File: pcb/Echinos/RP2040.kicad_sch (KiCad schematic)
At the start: 28 parts, among them SW224 Boot, SW225 Boot, SW226 Reset, SW227 Reset, U200 W25Q128JVP, U201 RP2040, Y200 Crystal_GND24

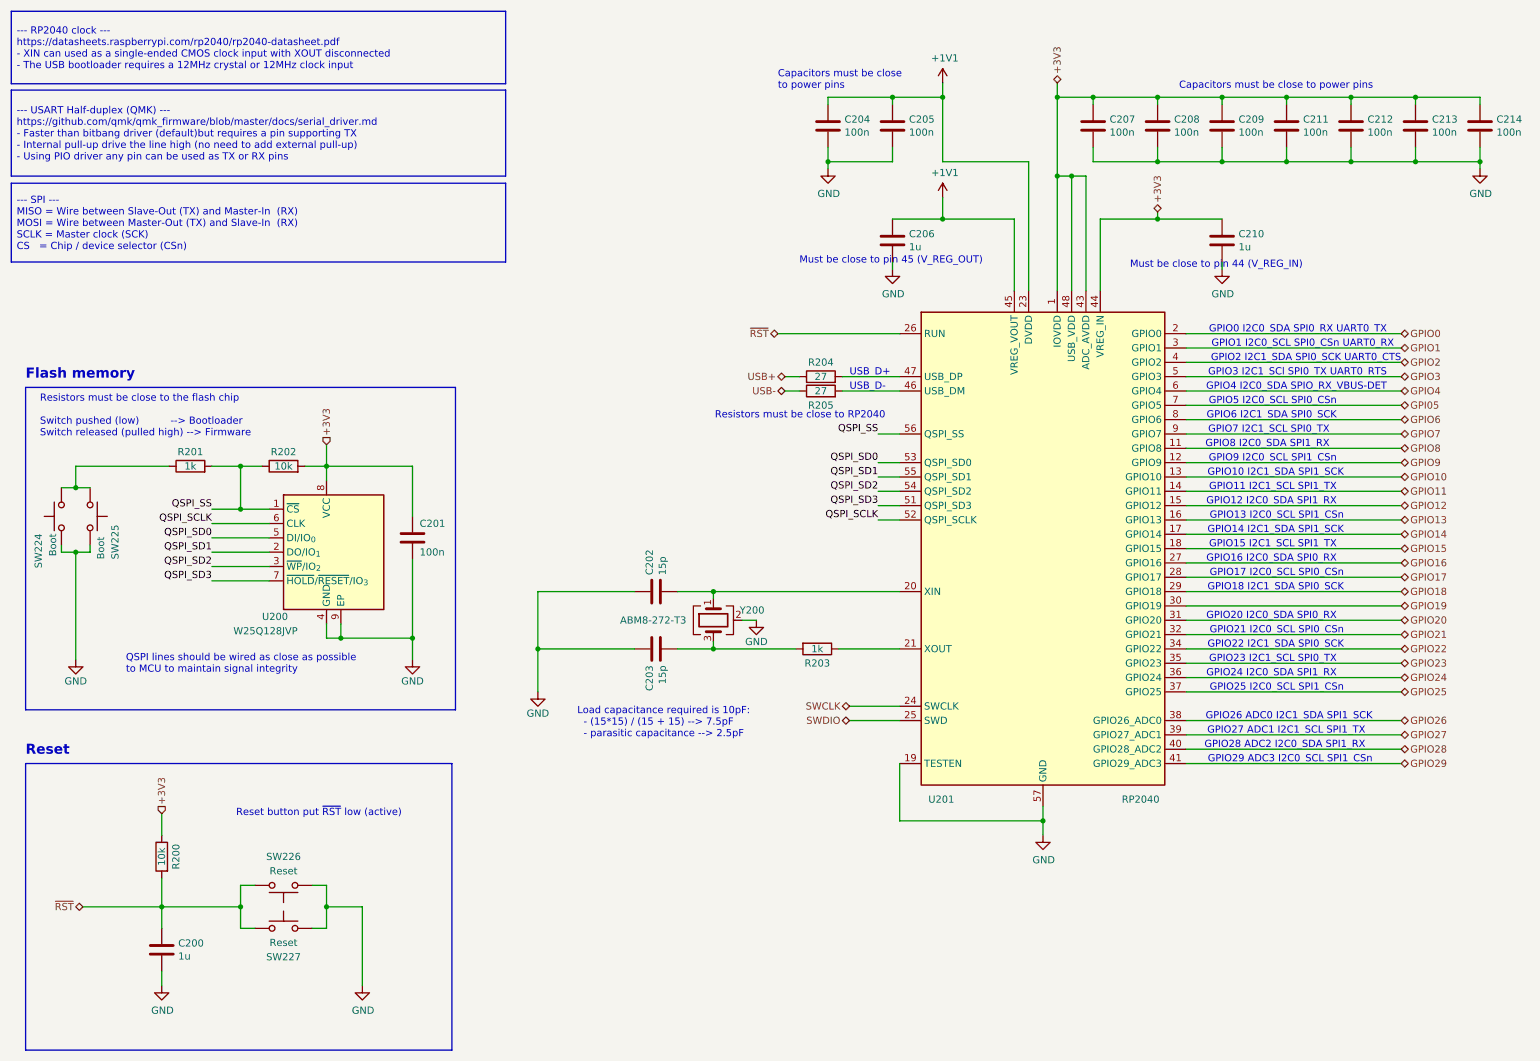
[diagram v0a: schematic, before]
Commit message: [PCB] - Save last state with on board RP2040.   - Fix flash component orientation for JLCPCB assembly   - Add logo + version   - Add TH in flash footprint and use the same zone fill method as for RP2040 footprint   - Improve ground planes under switches (right side)   - Move unused schematics to backup folder (will be used to create keyboard modules later)   - Add manufacturer and part name (mfr)   - Mark optional parts as DNP   - Resync with official RP2040 symbol and update pins matching
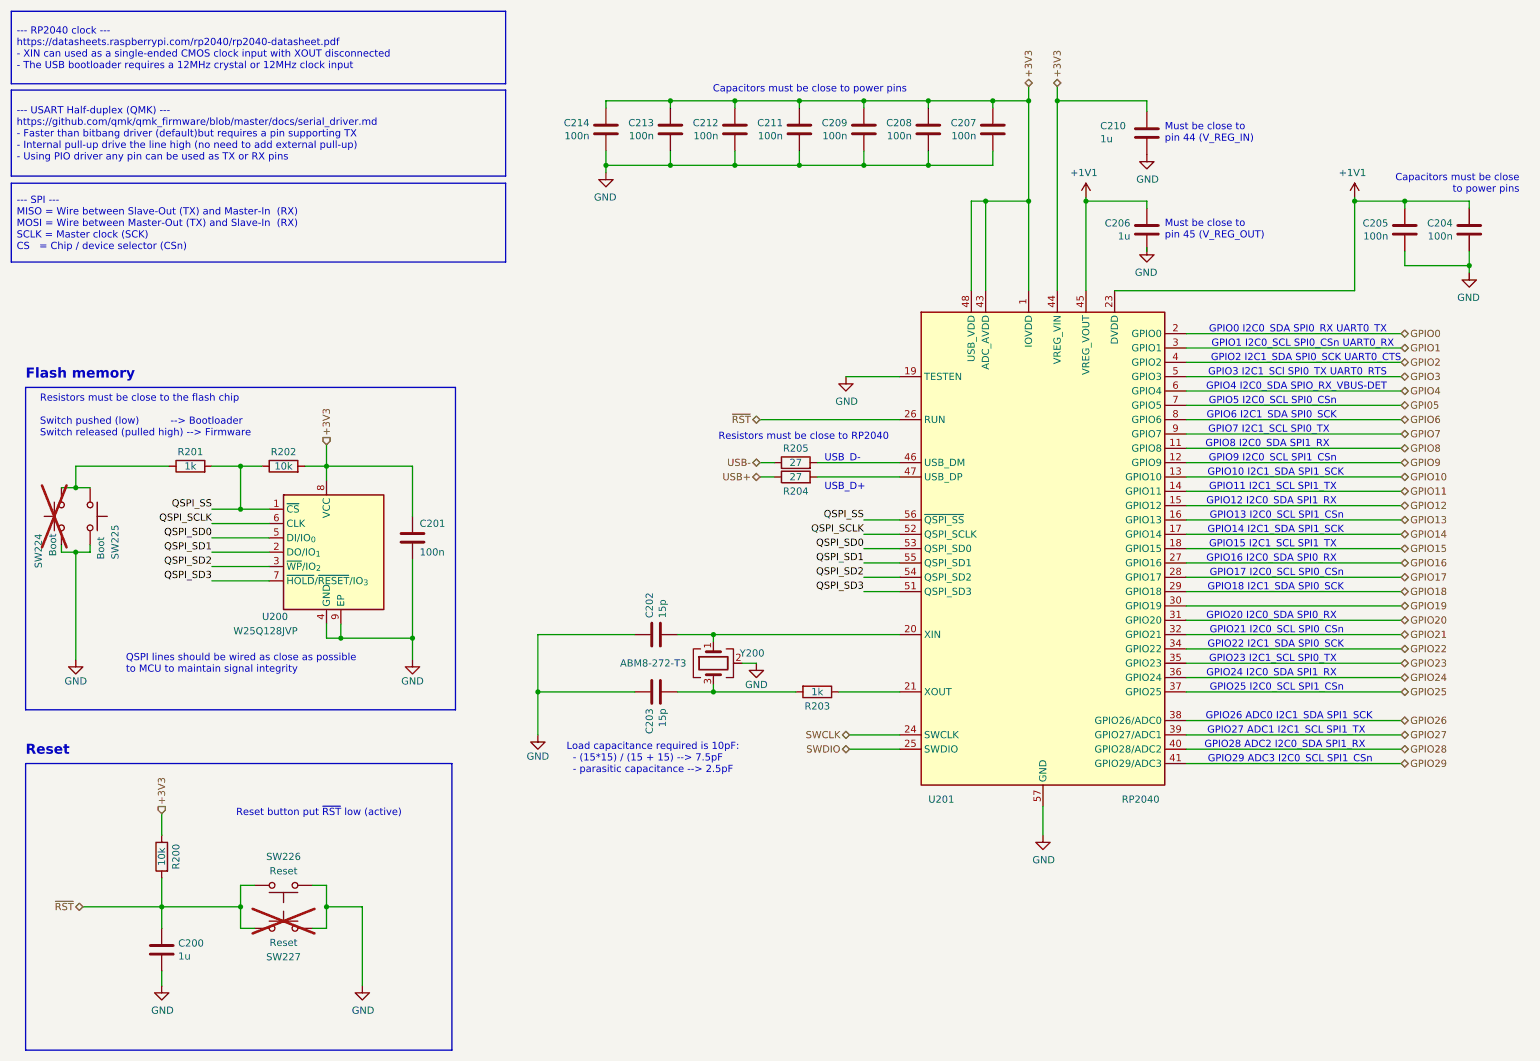
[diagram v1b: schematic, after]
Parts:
- C200, C206, C210: MFR (none) -> CL05A105KP5NNNC; Manufacturer (none) -> Samsung Electro-Mechanics
- C201: MFR (none) -> CL21B104KBCNNNC; Manufacturer (none) -> Samsung Electro-Mechanics
- C202, C203: MFR (none) -> CL05C150JB5NNNC; Manufacturer (none) -> Samsung Electro-Mechanics
- C204, C205, C207, C208, C209, C211, C212, C213, C214: MFR (none) -> CL05B104KO5NNNC; Manufacturer (none) -> Samsung Electro-Mechanics
- R200, R202: MFR (none) -> 0402WGF1002TCE; Manufacturer (none) -> UNI-ROYAL(Uniroyal Elec)
- R201, R203: MFR (none) -> 0402WGF1001TCE; Manufacturer (none) -> UNI-ROYAL(Uniroyal Elec)
- R204, R205: MFR (none) -> 0402WGF270JTCE; Manufacturer (none) -> UNI-ROYAL(Uniroyal Elec)
- SW224, SW227: MFR (none) -> TS-1088-AR02016; Manufacturer (none) -> XUNPU; now not fitted
- SW225, SW226: MFR (none) -> TS-1088-AR02016; Manufacturer (none) -> XUNPU
- U200: footprint Package_SON:WSON-8-1EP_6x5mm_P1.27mm_EP3.4x4mm -> Echinos:WSON-8-1EP_6x5mm_P1.27mm_EP3.4x4mm; FT Rotation Offset (none) -> 270; MFR (none) -> W25Q128JVPIQ; Manufacturer (none) -> Winbond Elec
- U201: MFR (none) -> RP2040; Manufacturer (none) -> Raspberry Pi
- Y200: MFR (none) -> ABM8-272-T3; Manufacturer (none) -> Abracon LLC
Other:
- moved on the sheet: C202, C203, C204, C205, C206, C207, C208, C209, C210, C211, C212, C213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

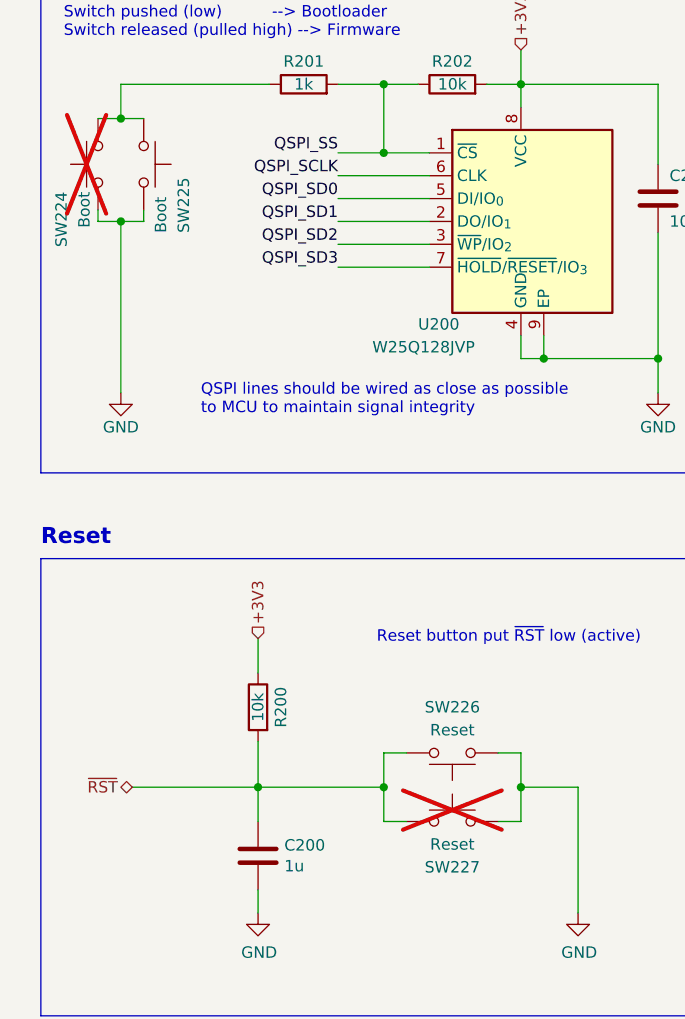
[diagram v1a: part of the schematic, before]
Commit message: [PCB] - Save last state with on board RP2040.   - Move to kicad 10   - Add DRC custom rule to exclude errors on PTH for switches due to holes being too close   - Move thermal via in both RP2040 and Flash memory to pad corners (better for manufacturing)   - Update USB footprint to match changes in kicad associated symbol   - Increase trackpoint holes from 3.0 to 3.2mm (cannot do more I guess)   - Removed unused footprint from library
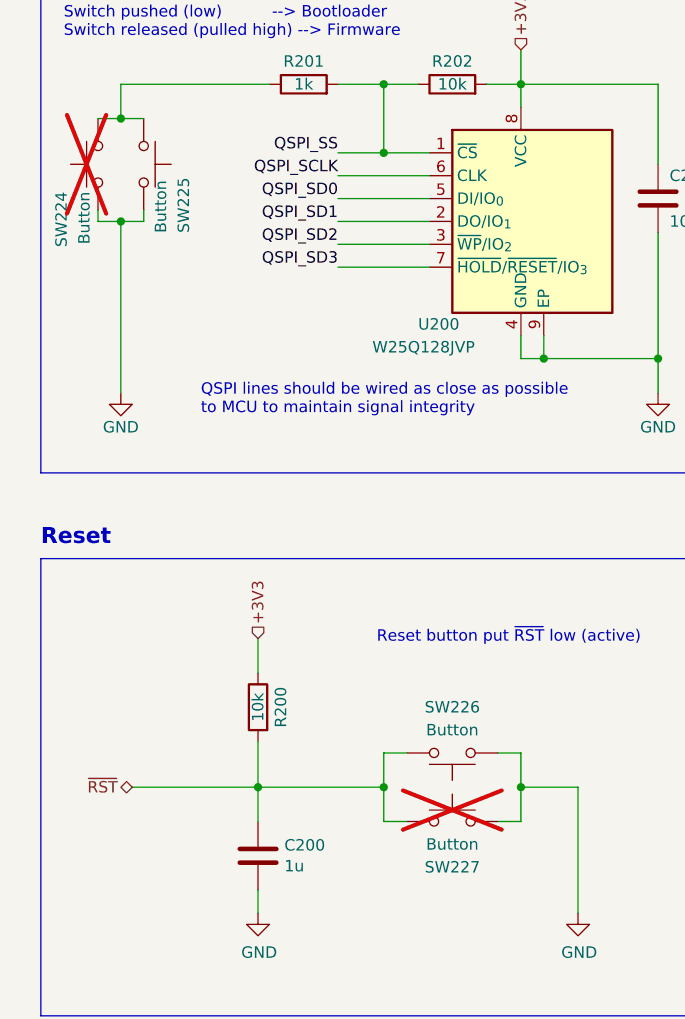
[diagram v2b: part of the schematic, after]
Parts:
- SW224, SW225: value Boot -> Button
- SW226, SW227: value Reset -> Button
- U201: footprint Echinos:RP2040-QFN-56 -> Echinos:QFN-56-1EP_7x7mm_P0.4mm_EP3.2x3.2mm_ThermalVias; FT Rotation Offset (none) -> 270
